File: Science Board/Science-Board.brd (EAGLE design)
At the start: 104.1 x 55.9 mm, 66 parts, among them U3 SN74AHCT125

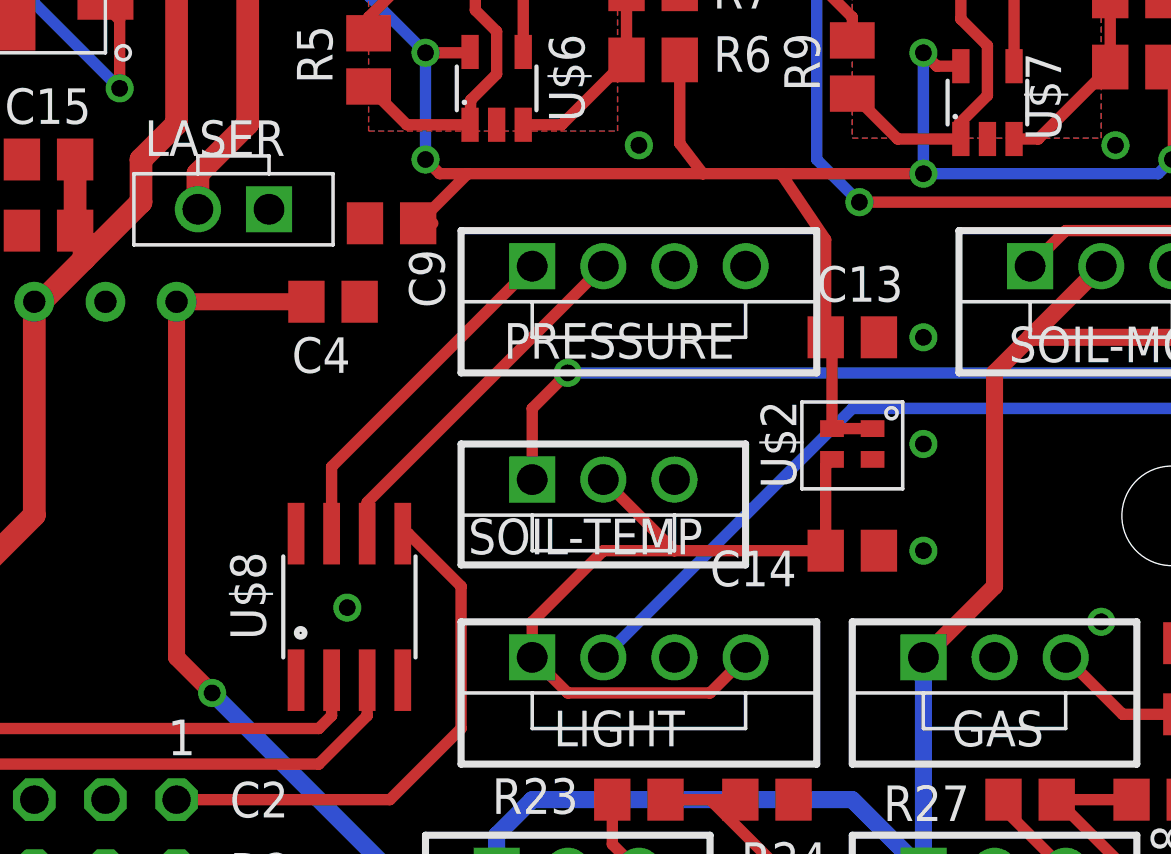
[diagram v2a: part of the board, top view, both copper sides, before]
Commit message: Fixed ERC errors
a couple of things weren't properly conencted in schematic. Fixed those and corresponding pcb changes
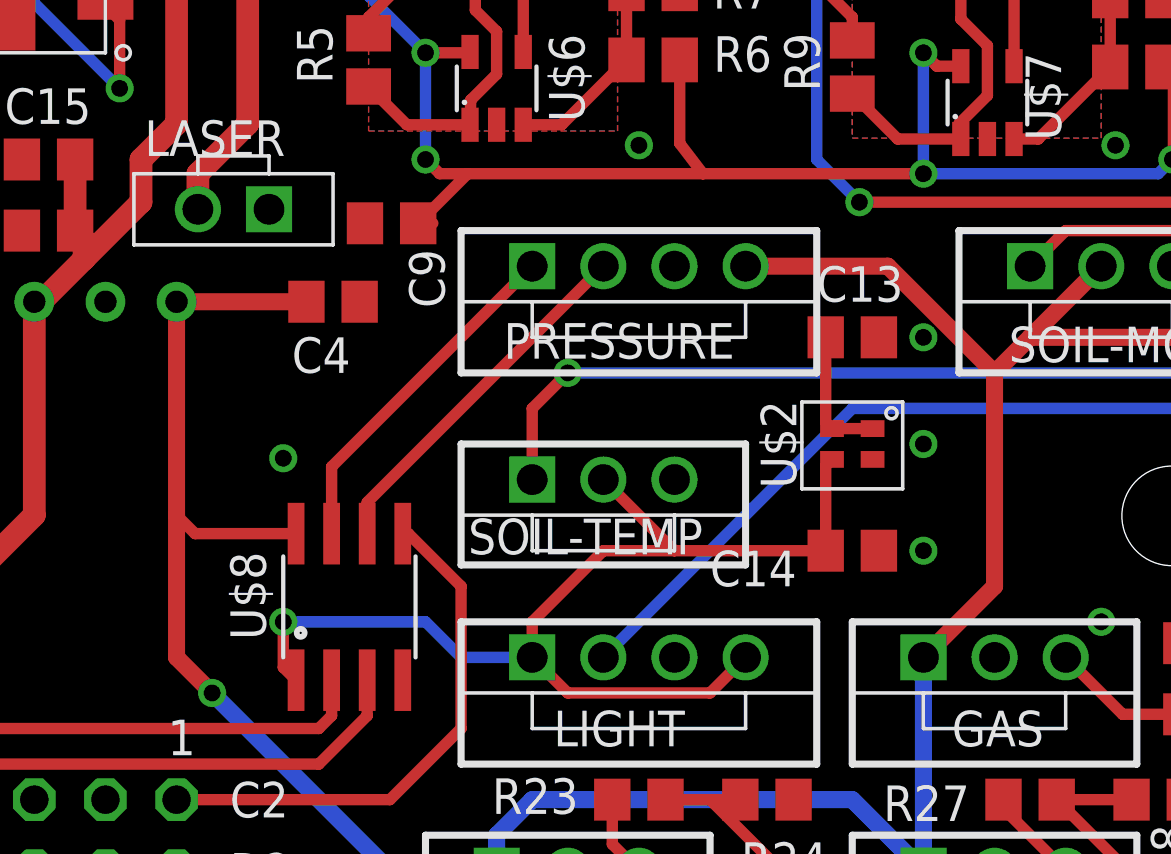
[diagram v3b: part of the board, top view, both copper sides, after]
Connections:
- removed net 3V-ENABLE: U$1.PK7
- removed net EN: U$1.PP3
- removed net PHASE: U$1.PQ1
- removed net SLEEP: U$1.PM6
- removed net UV-3.3: C14.1, LIGHT.1, LIGHT.4, SOIL-TEMP.2, U$2.P$3
- net 3.3V: now also C14.1, LIGHT.1, LIGHT.4, SOIL-TEMP.2, U$2.P$3
- net 5V-EXT: now also C13.1, PRESSURE.4, U$2.P$1, U$2.P$2, U$8.8
- net 5V-INT: no longer C13.1, U$2.P$1, U$2.P$2
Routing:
- net 3.3V: track 0.00 -> 40.1 mm, vias 0 -> 1
- net UV-3.3: track 28.4 -> 0.00 mm
- net 5V-EXT: track 140.6 -> 160.4 mm
- net 5V-INT: track 135.4 -> 124.2 mm
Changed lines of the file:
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@@
 <?xml version="1.0" encoding="utf-8"?>
 <!DOCTYPE eagle SYSTEM "eagle.dtd">
-<eagle version="6.5.0">
+<eagle version="7.7.0">
 <drawing>
 <settings>
@@
 <pass name="Default">
 <param name="RoutingGrid" value="50mil"/>
+<param name="AutoGrid" value="1"/>
+<param name="Efforts" value="0"/>
+<param name="TopRouterVariant" value="1"/>
 <param name="tpViaShape" value="round"/>
 <param name="PrefDir.1" value="|"/>
@@
 <via x="2.54" y="53.594" extent="1-16" drill="0.6" shape="square"/>
 <via x="2.54" y="39.878" extent="1-16" drill="0.6" shape="square"/>
-<via x="42.926" y="14.478" extent="1-16" drill="0.6" shape="square"/>
+<via x="40.64" y="19.812" extent="1-16" drill="0.6" shape="square"/>
 <via x="57.15" y="2.54" extent="1-16" drill="0.6" shape="square"/>
 <via x="74.93" y="6.35" extent="1-16" drill="0.6" shape="square"/>
@@
 <via x="53.34" y="30.988" extent="1-16" drill="0.6" shape="square"/>
 <via x="70.358" y="30.988" extent="1-16" drill="0.6" shape="square"/>
-</signal>
-<signal name="PHASE">
-<contactref element="U$1" pad="PQ1"/>
-</signal>
-<signal name="EN">
-<contactref element="U$1" pad="PP3"/>
-</signal>
-<signal name="SLEEP">
-<contactref element="U$1" pad="PM6"/>
 </signal>
 <signal name="5V-EXT">
@@
 <wire x1="78.232" y1="20.988" x2="78.232" y2="23.368" width="0.6096" layer="1"/>
 <wire x1="78.232" y1="23.368" x2="77.47" y2="24.13" width="0.6096" layer="1"/>
-<wire x1="36.83" y1="25.4" x2="36.83" y2="12.7" width="0.6096" layer="1"/>
+<wire x1="36.83" y1="25.4" x2="36.83" y2="17.78" width="0.6096" layer="1"/>
+<wire x1="36.83" y1="17.78" x2="36.83" y2="12.7" width="0.6096" layer="1"/>
 <wire x1="36.83" y1="12.7" x2="38.1" y2="11.43" width="0.6096" layer="1"/>
 <via x="38.1" y="11.43" extent="1-16" drill="0.6"/>
@@
 <wire x1="95.25" y1="27.94" x2="95.25" y2="18.542" width="0.6096" layer="1"/>
 <wire x1="95.25" y1="18.542" x2="92.71" y2="16.002" width="0.6096" layer="1"/>
+<contactref element="U$8" pad="8"/>
+<contactref element="PRESSURE" pad="4"/>
+<wire x1="41.097" y1="17.1192" x2="37.4908" y2="17.1192" width="0.4064" layer="1"/>
+<wire x1="37.4908" y1="17.1192" x2="36.83" y2="17.78" width="0.4064" layer="1"/>
+<contactref element="U$2" pad="P$1"/>
+<contactref element="C13" pad="1"/>
+<contactref element="U$2" pad="P$2"/>
+<wire x1="60.01" y1="24.13" x2="60.01" y2="21.095" width="0.4064" layer="1"/>
+<wire x1="60.01" y1="21.095" x2="60.235" y2="20.87" width="0.4064" layer="1"/>
+<wire x1="60.235" y1="20.87" x2="61.685" y2="20.87" width="0.4064" layer="1"/>
+<wire x1="57.15" y1="26.67" x2="62.23" y2="26.67" width="0.6096" layer="1"/>
+<wire x1="62.23" y1="26.67" x2="66.04" y2="22.86" width="0.6096" layer="1"/>
+<wire x1="62.23" y1="26.67" x2="60.01" y2="24.13" width="0" layer="19" extent="1-1"/>
 </signal>
 <signal name="5V-INT">
@@
 <contactref element="U$1" pad="+5V_1" route="any" routetag="G$1.+5V"/>
 <contactref element="U$1" pad="+5V_2" route="any" routetag="G$1.+5V"/>
-<contactref element="U$2" pad="P$2"/>
-<contactref element="C13" pad="1"/>
-<contactref element="U$2" pad="P$1"/>
 <contactref element="R14" pad="2"/>
 <wire x1="36.83" y1="48.26" x2="38.1" y2="48.26" width="0.6096" layer="16"/>
@@
 <wire x1="6.03" y1="48.26" x2="7.62" y2="48.26" width="0.6096" layer="1"/>
 <wire x1="43.688" y1="36.322" x2="43.688" y2="46.482" width="0.4064" layer="16"/>
-<wire x1="60.235" y1="20.87" x2="61.685" y2="20.87" width="0.4064" layer="1"/>
 <wire x1="6.096" y1="42.164" x2="6.604" y2="42.164" width="0.6096" layer="1"/>
 <wire x1="6.604" y1="42.164" x2="7.62" y2="43.18" width="0.6096" layer="1"/>
@@
 <wire x1="3.81" y1="44.45" x2="2.86" y2="44.45" width="0.4064" layer="1"/>
 <wire x1="2.86" y1="44.45" x2="2.54" y2="44.13" width="0.4064" layer="1"/>
-<wire x1="63.5" y1="29.972" x2="58.42" y2="29.972" width="0.4064" layer="1"/>
-<wire x1="58.42" y1="29.972" x2="55.626" y2="29.972" width="0.4064" layer="1"/>
+<wire x1="63.5" y1="29.972" x2="55.626" y2="29.972" width="0.4064" layer="1"/>
 <wire x1="55.626" y1="29.972" x2="47.228" y2="29.972" width="0.4064" layer="1"/>
 <wire x1="45.458" y1="28.202" x2="45.982" y2="28.202" width="0.4064" layer="1"/>
@@
 <wire x1="63.5" y1="34.29" x2="63.5" y2="29.972" width="0.4064" layer="16"/>
 <via x="63.5" y="29.972" extent="1-16" drill="0.6"/>
-<wire x1="60.235" y1="20.87" x2="60.235" y2="23.905" width="0.4064" layer="1"/>
-<wire x1="60.235" y1="23.905" x2="60.01" y2="24.13" width="0.4064" layer="1"/>
-<wire x1="60.01" y1="24.13" x2="60.01" y2="27.62" width="0.4064" layer="1"/>
-<wire x1="60.01" y1="27.62" x2="58.42" y2="29.972" width="0.4064" layer="1"/>
 <wire x1="47.228" y1="29.972" x2="45.458" y2="28.202" width="0.4064" layer="1"/>
 <wire x1="47.228" y1="29.972" x2="46.228" y2="29.972" width="0.4064" layer="1"/>
@@
 <wire x1="83.312" y1="15.588" x2="83.312" y2="9.398" width="0.4064" layer="1"/>
 <wire x1="83.312" y1="9.398" x2="85.09" y2="7.62" width="0.4064" layer="1"/>
-</signal>
-<signal name="3V-ENABLE">
-<contactref element="U$1" pad="PK7"/>
 </signal>
 <signal name="N$4">
@@
 <signal name="3.3V">
 <contactref element="U$8" pad="1"/>
+<contactref element="U$2" pad="P$3"/>
+<contactref element="C14" pad="1"/>
+<contactref element="LIGHT" pad="1"/>
+<contactref element="LIGHT" pad="4"/>
+<contactref element="SOIL-TEMP" pad="2"/>
+<wire x1="60.01" y1="16.51" x2="60.01" y2="19.545" width="0.4064" layer="1"/>
+<wire x1="60.01" y1="19.545" x2="60.235" y2="19.77" width="0.4064" layer="1"/>
+<wire x1="60.01" y1="16.51" x2="54.61" y2="16.51" width="0.4064" layer="1"/>
+<wire x1="54.61" y1="16.51" x2="52.07" y2="19.05" width="0.4064" layer="1"/>
+<wire x1="54.61" y1="16.51" x2="52.07" y2="16.51" width="0.4064" layer="1"/>
+<wire x1="52.07" y1="16.51" x2="49.53" y2="13.97" width="0.4064" layer="1"/>
+<wire x1="49.53" y1="13.97" x2="49.53" y2="12.7" width="0.4064" layer="1"/>
+<wire x1="57.15" y1="12.7" x2="55.88" y2="11.43" width="0.4064" layer="1"/>
+<wire x1="55.88" y1="11.43" x2="50.8" y2="11.43" width="0.4064" layer="1"/>
+<wire x1="50.8" y1="11.43" x2="49.53" y2="12.7" width="0.4064" layer="1"/>
+<wire x1="49.53" y1="12.7" x2="46.99" y2="12.7" width="0.4064" layer="16"/>
+<wire x1="46.99" y1="12.7" x2="45.72" y2="13.97" width="0.4064" layer="16"/>
+<wire x1="45.72" y1="13.97" x2="40.64" y2="13.97" width="0.4064" layer="16"/>
+<via x="40.64" y="13.97" extent="1-16" drill="0.6"/>
+<wire x1="40.64" y1="13.97" x2="40.64" y2="12.3438" width="0.4064" layer="1"/>
+<wire x1="40.64" y1="12.3438" x2="41.097" y2="11.8868" width="0.4064" layer="1"/>
 </signal>
 <signal name="PRESSURE-SDA-3V3">
@@
 <wire x1="89.9894" y1="41.958" x2="90.9066" y2="42.8752" width="0.4064" layer="1"/>
 </signal>
-<signal name="UV-3.3">
-<contactref element="U$2" pad="P$3"/>
-<contactref element="C14" pad="1"/>
-<contactref element="LIGHT" pad="1"/>
-<contactref element="LIGHT" pad="4"/>
-<contactref element="SOIL-TEMP" pad="2"/>
-<wire x1="60.01" y1="16.51" x2="60.01" y2="19.545" width="0.4064" layer="1"/>
-<wire x1="60.01" y1="19.545" x2="60.235" y2="19.77" width="0.4064" layer="1"/>
-<wire x1="60.01" y1="16.51" x2="54.61" y2="16.51" width="0.4064" layer="1"/>
-<wire x1="54.61" y1="16.51" x2="52.07" y2="19.05" width="0.4064" layer="1"/>
-<wire x1="54.61" y1="16.51" x2="52.07" y2="16.51" width="0.4064" layer="1"/>
-<wire x1="52.07" y1="16.51" x2="49.53" y2="13.97" width="0.4064" layer="1"/>
-<wire x1="49.53" y1="13.97" x2="49.53" y2="12.7" width="0.4064" layer="1"/>
-<wire x1="57.15" y1="12.7" x2="55.88" y2="11.43" width="0.4064" layer="1"/>
-<wire x1="55.88" y1="11.43" x2="50.8" y2="11.43" width="0.4064" layer="1"/>
-<wire x1="50.8" y1="11.43" x2="49.53" y2="12.7" width="0.4064" layer="1"/>
-</signal>
 <signal name="N$21">

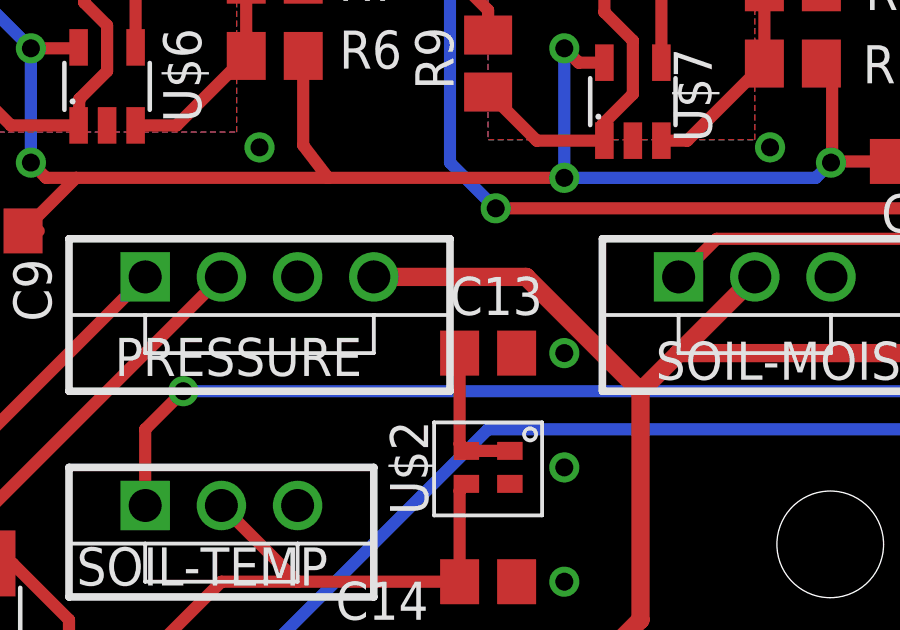
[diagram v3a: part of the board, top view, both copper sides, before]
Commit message: ONE MORE I SWEAR
fixed airwire.
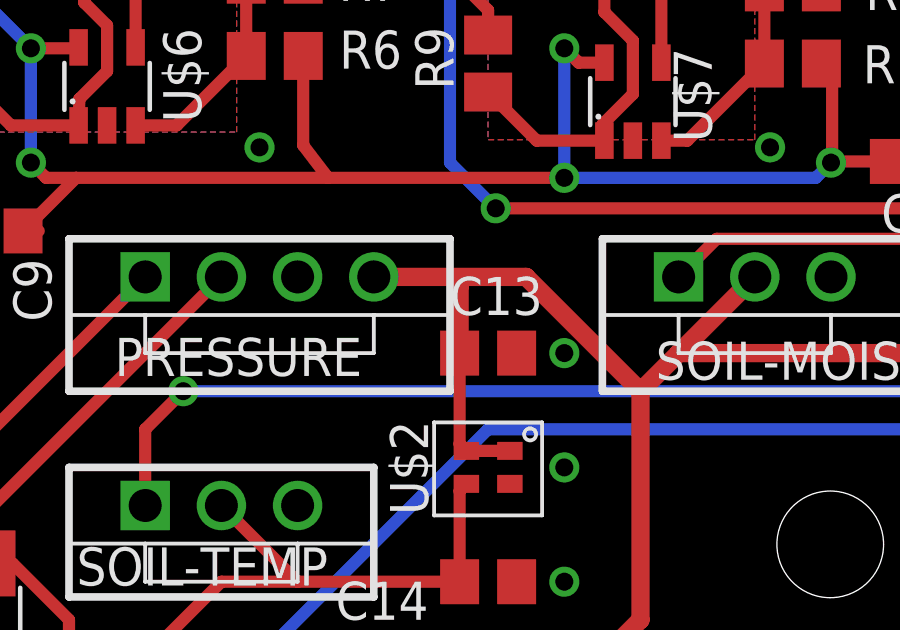
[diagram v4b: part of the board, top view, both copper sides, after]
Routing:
- net 5V-EXT: track 160.4 -> 163.0 mm
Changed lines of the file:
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@@
 <wire x1="60.01" y1="21.095" x2="60.235" y2="20.87" width="0.4064" layer="1"/>
 <wire x1="60.235" y1="20.87" x2="61.685" y2="20.87" width="0.4064" layer="1"/>
-<wire x1="57.15" y1="26.67" x2="62.23" y2="26.67" width="0.6096" layer="1"/>
+<wire x1="57.15" y1="26.67" x2="59.69" y2="26.67" width="0.6096" layer="1"/>
+<wire x1="59.69" y1="26.67" x2="62.23" y2="26.67" width="0.6096" layer="1"/>
 <wire x1="62.23" y1="26.67" x2="66.04" y2="22.86" width="0.6096" layer="1"/>
-<wire x1="62.23" y1="26.67" x2="60.01" y2="24.13" width="0" layer="19" extent="1-1"/>
+<wire x1="60.01" y1="24.13" x2="60.01" y2="26.35" width="0.6096" layer="1"/>
+<wire x1="60.01" y1="26.35" x2="59.69" y2="26.67" width="0.6096" layer="1"/>
 </signal>
 <signal name="5V-INT">

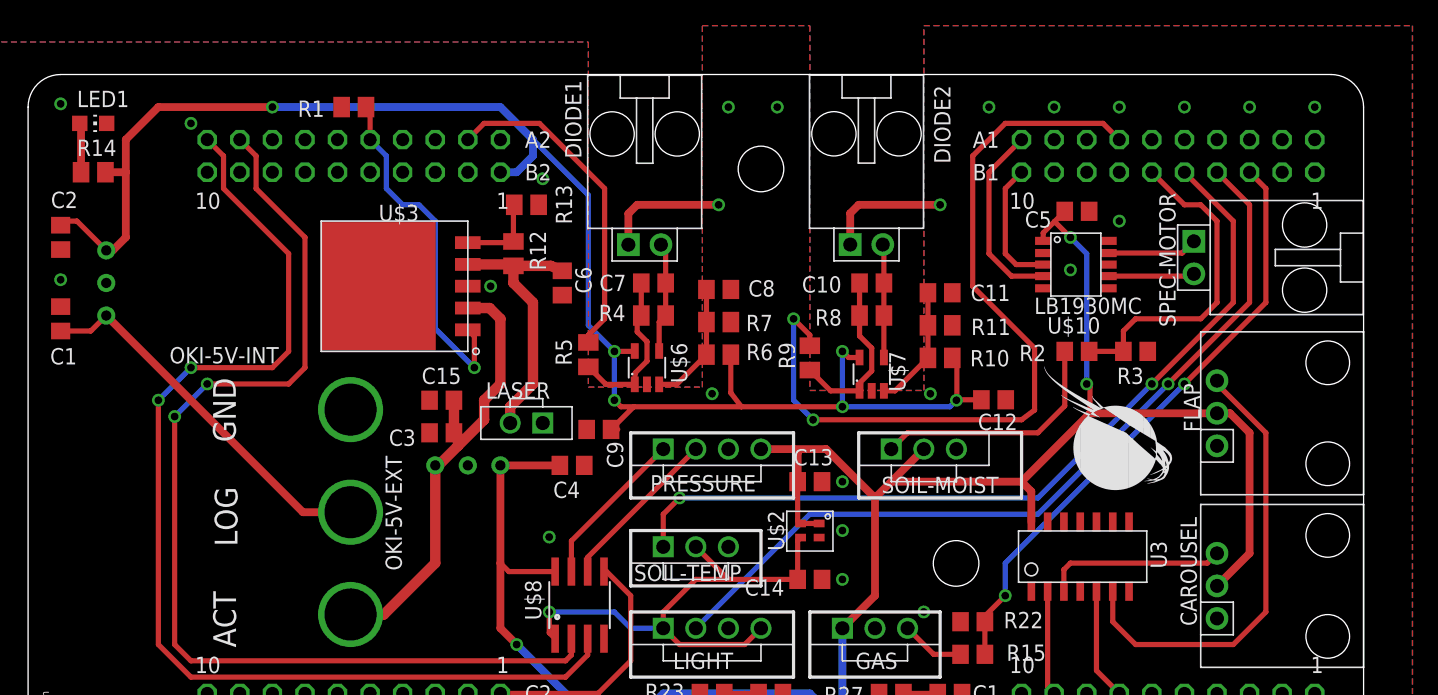
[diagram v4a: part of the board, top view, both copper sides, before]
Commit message: I think that's everything
Moved upper mounting hole, nudged Diode2 circuit to the right to make room, fixed labels in schematic, fixed scattered vias
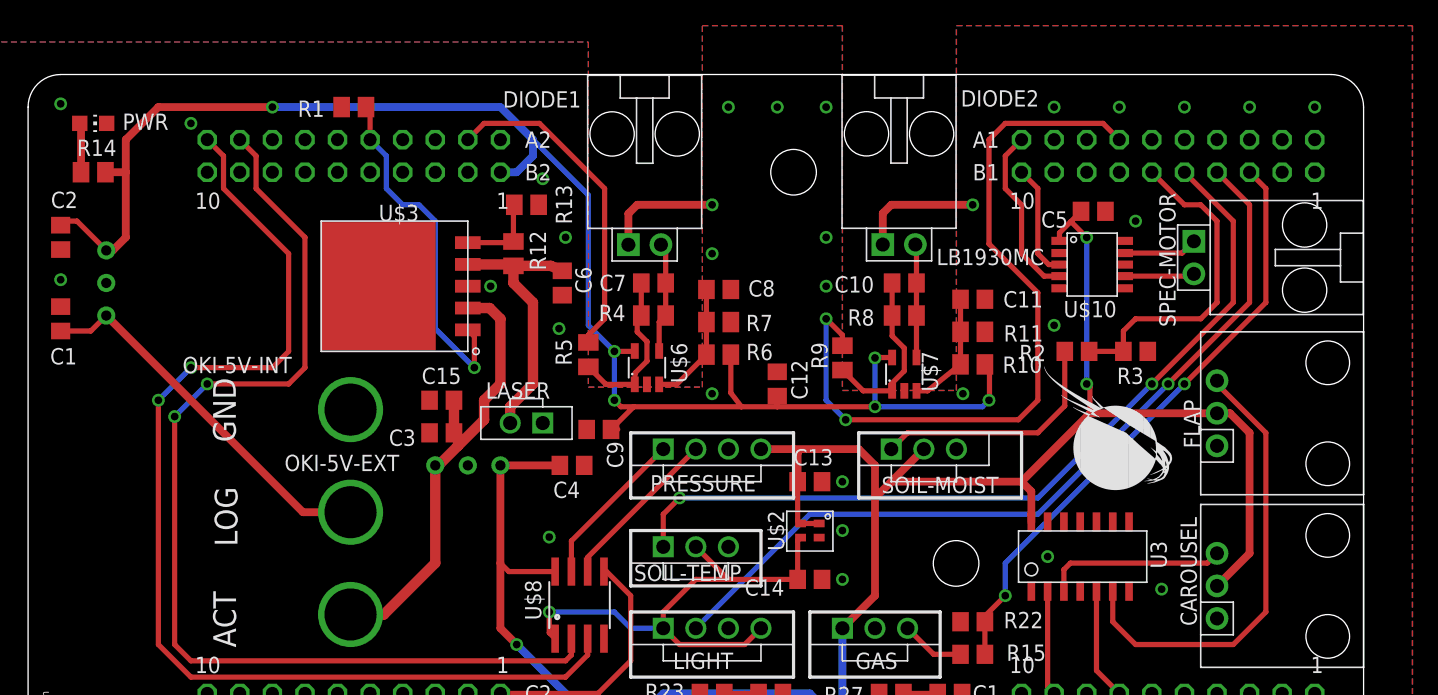
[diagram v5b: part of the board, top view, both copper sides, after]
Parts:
- moved C12 16.9 mm to (58.4, 31.8), turned to 270 degrees
- moved C11 2.59 mm to (73.7, 38.4)
- moved R11 2.59 mm to (73.7, 35.8)
- moved R10 2.59 mm to (73.7, 33.3)
- moved H3 2.55 mm to (59.7, 48.3)
- moved DIODE2 2.54 mm to (67.9, 42.6)
- moved R9 2.54 mm to (63.5, 33.8)
- moved C10 2.54 mm to (68.3, 39.6)
- moved R8 2.54 mm to (68.3, 37.1)
- moved U$7 2.54 mm to (68.3, 32.5)
- moved C5 1.27 mm to (83.1, 45.2)
- moved U$10 1.27 mm to (81.0, 38.6)
- renumbered LED1 to PWR
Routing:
- net PHOTO-IN-2: track 63.5 -> 59.9 mm
- net N$2: track 7.03 -> 5.76 mm
- net N$1: track 6.72 -> 5.45 mm
- net IN2: track 14.9 -> 13.6 mm
- net IN1: track 10.2 -> 8.91 mm
- net 5V-EXT: track 163.0 -> 164.0 mm
- net GND: track 19.5 -> 19.0 mm, vias 38 -> 44
